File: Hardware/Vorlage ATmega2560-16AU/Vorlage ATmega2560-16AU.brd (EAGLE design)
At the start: 160 x 100 mm, 118 parts, among them IC1 CD74HC14PW, IC2 ATMEGA2560640V-8AU, IC3 SS39E, IC4 SS39E, IC5 74AC138D, IC6 XC6210B332MR, Q1 16MHz, Q10 PMV27UPER, Q2 32.768kHz, Q3 PMV27UPER, Q4 PMV27UPER, Q5 PMV27UPER, Q6 PMV27UPER, Q7 PMV27UPER, Q8 PMV27UPER, Q9 PMV27UPER, U1 LM35DZ, X1 2510-, X2 +5V, X3 2514-, X4 2510-

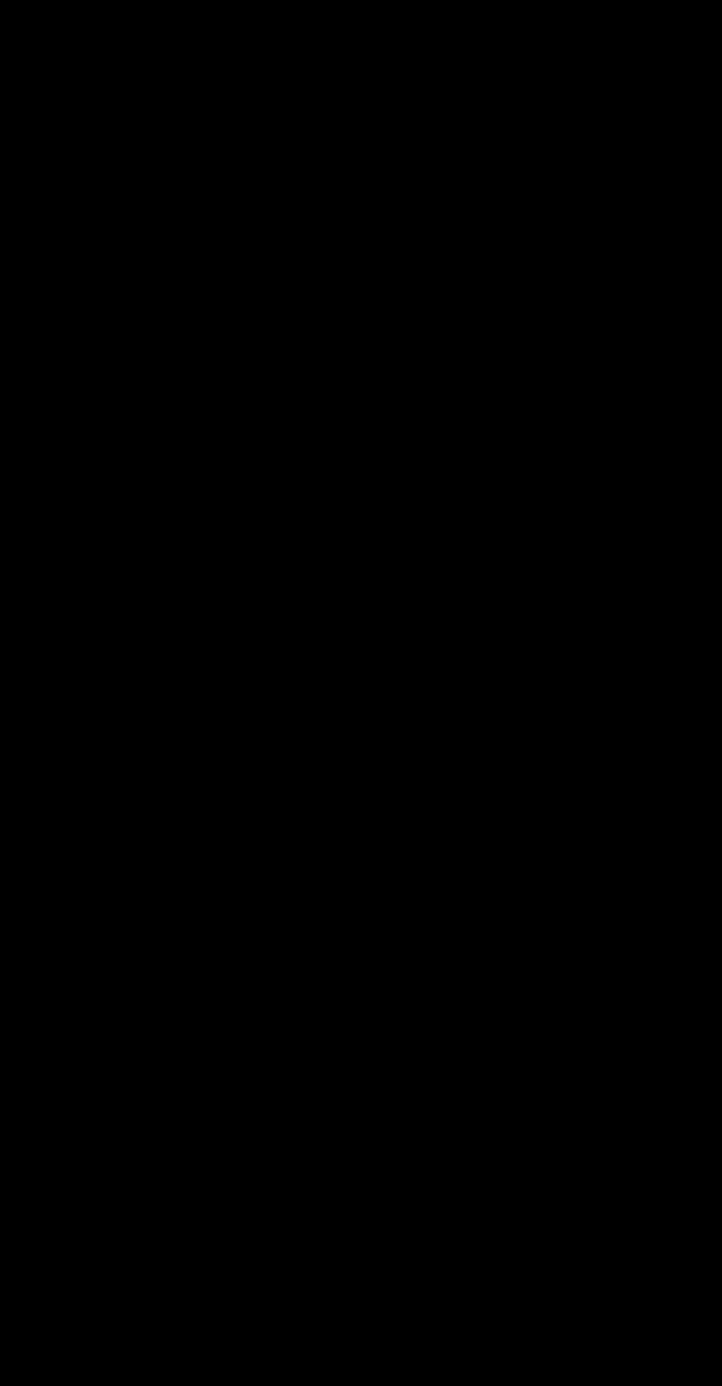
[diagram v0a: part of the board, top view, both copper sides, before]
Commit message: LEDs neu über FET
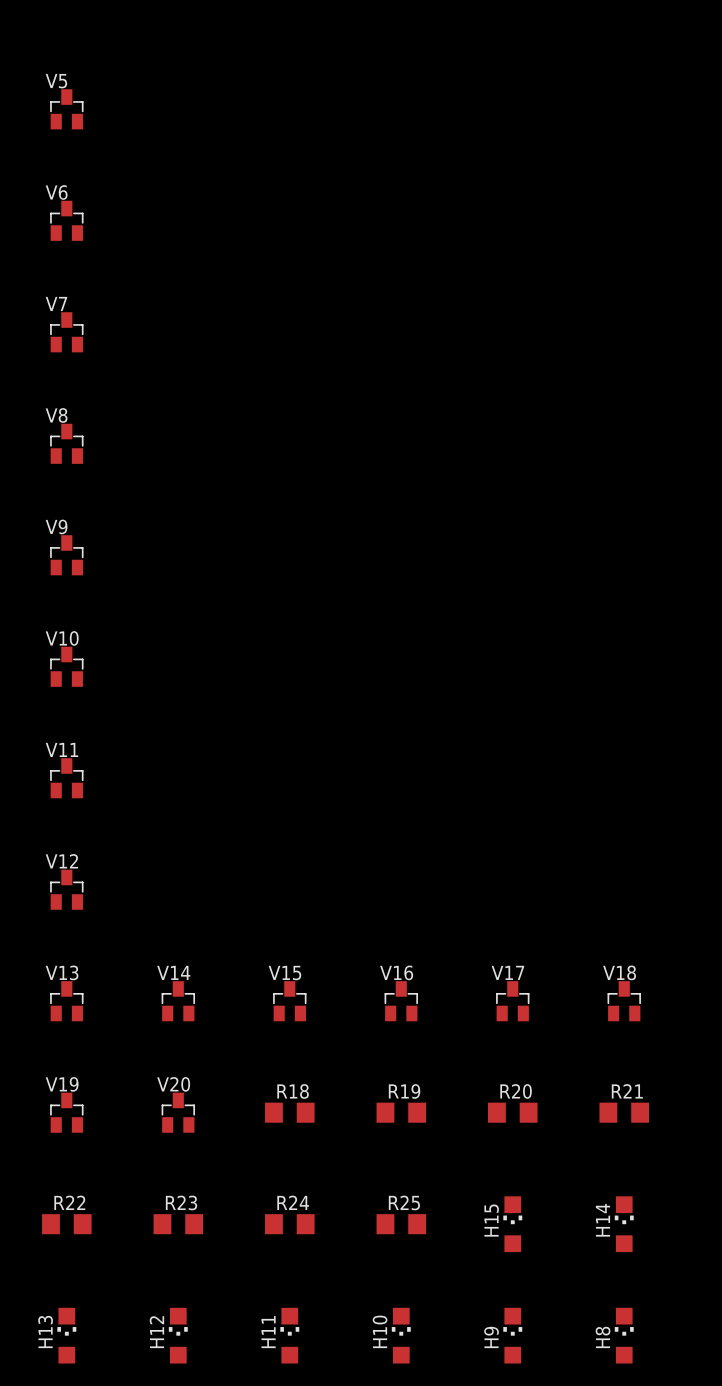
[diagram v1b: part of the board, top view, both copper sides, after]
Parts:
- added H10, H11, H12, H13, H14, H15, H8, H9: blau, led:CHIPLED_1206
- added R18, R19, R20, R21, R22, R23, R24, R25: 150R, rcl:R1206
- added V10, V11, V12, V13, V14, V15, V16, V17, V18, V19, V20, V5, V6, V7, V8, V9: PMV20EN, transistor-fet-mit-BSS138:SOT23
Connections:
- new net H1: H15.C, R19.2
- new net N$13: R33.1, V8.3
- new net N$14: R32.1, V9.3
- new net N$15: R31.1, V10.3
- new net N$16: R30.1, V11.3
- new net N$17: R29.1, V12.3
- new net N$45: IC2.78, V5.1
- new net N$46: H14.C, R18.2
- new net N$47: H12.C, R20.2
- new net N$51: H13.C, R21.2
- new net N$52: H10.C, R22.2
- new net N$55: H11.C, R23.2
- new net N$56: H8.C, R24.2
- new net N$59: H9.C, R25.2
- new net N$61: R24.1, V13.3
- new net N$63: R25.1, V14.3
- new net N$69: R19.1, V20.3
- new net N$71: IC2.77, V6.1
- new net N$72: IC2.76, V7.1
- new net N$74: IC2.75, V8.1
- new net N$76: IC2.74, V9.1
- new net N$77: IC2.73, V10.1
- new net N$78: IC2.72, V11.1
- new net N$79: IC2.71, V12.1
- new net N$80: IC2.19, V13.1
- new net N$81: IC2.20, V14.1
- new net N$82: IC2.21, V15.1
- new net N$83: IC2.22, V16.1
- new net N$84: IC2.23, V17.1
- new net N$85: IC2.24, V18.1
- new net N$86: IC2.25, V19.1
- new net N$87: IC2.26, V20.1
- net GND: now also V10.2, V11.2, V12.2, V13.2, V14.2, V15.2, V16.2, V17.2, V18.2, V19.2, V20.2, V5.2, V6.2, V7.2, V8.2, V9.2
- net N$5: now also R36.1, V5.3; no longer IC2.71, R29.1
- net N$6: now also R35.1, V6.3; no longer IC2.72, R30.1
- net N$64: now also R22.1, V15.3; no longer IC2.78, R36.1
- net N$65: now also R23.1, V16.3; no longer IC2.77, R35.1
- net N$66: now also R20.1, V17.3; no longer IC2.76, R34.1
- net N$67: now also R21.1, V18.3; no longer IC2.75, R33.1
- net N$68: now also R18.1, V19.3; no longer IC2.74, R32.1
- net N$7: now also R34.1, V7.3; no longer IC2.73, R31.1
- net VCC: now also H10.A, H11.A, H12.A, H13.A, H14.A, H15.A, H8.A, H9.A

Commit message: Sicherung F1 ist 2A
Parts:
- F2: value 500mA -> 2A
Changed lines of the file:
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@@
 <attribute name="VALUE" x="-41.91" y="139.7" size="1.27" layer="27"/>
 </element>
-<element name="F2" library="fuse" package="F1206" value="500mA" x="-110.49" y="120.65" smashed="yes">
+<element name="F2" library="fuse" package="F1206" value="2A" x="-110.49" y="120.65" smashed="yes">
 <attribute name="NAME" x="-111.76" y="121.92" size="1.27" layer="25"/>
 <attribute name="VALUE" x="-111.76" y="118.11" size="1.27" layer="27"/>
